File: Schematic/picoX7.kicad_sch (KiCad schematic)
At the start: 8 parts, among them J1 MIDI in, J2 Debug serial, SW1 RST, U1 H11L1, U2 Pico, U3 I2S DAC

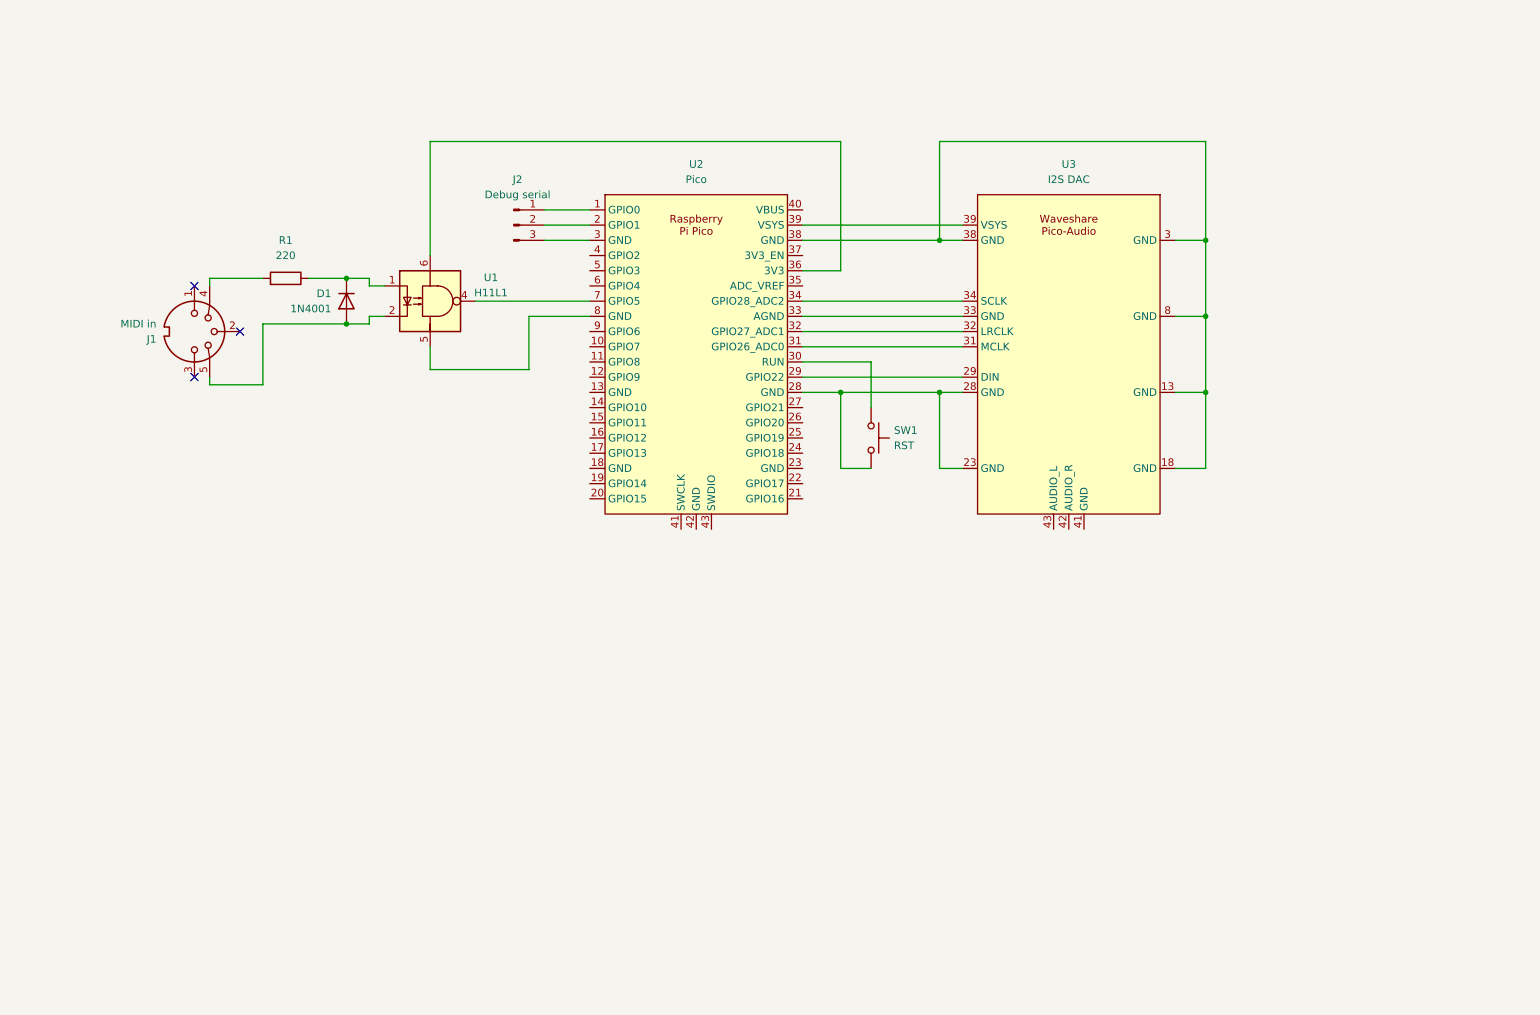
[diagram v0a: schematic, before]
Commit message: Update schematic with planned extensions
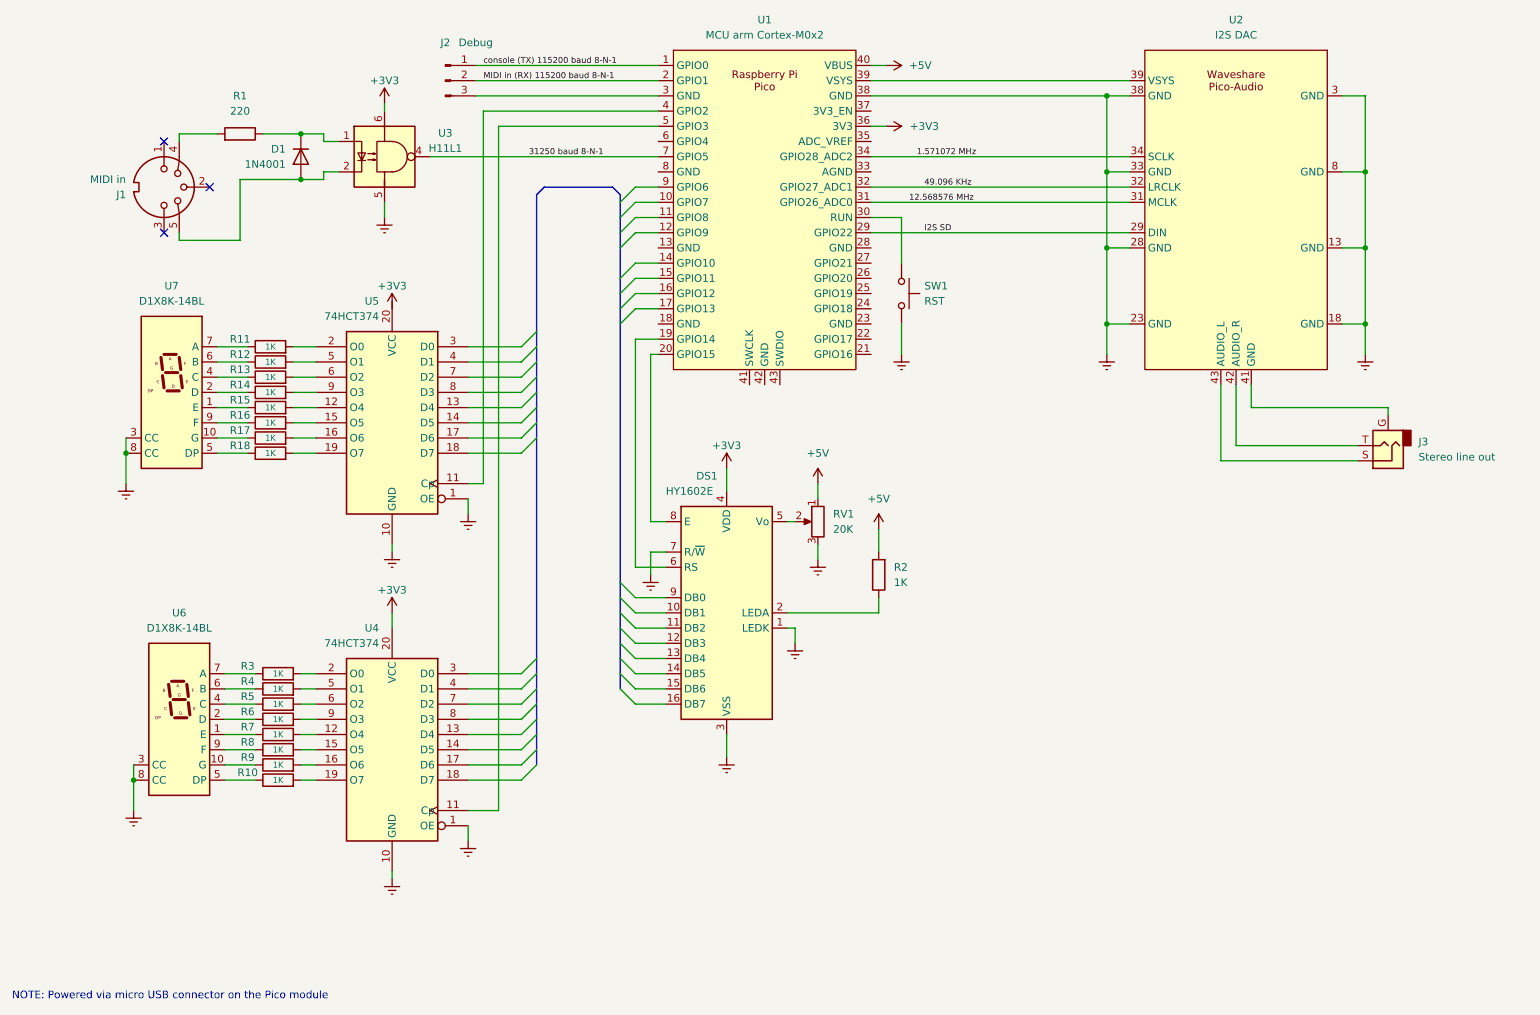
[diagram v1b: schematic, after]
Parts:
- added DS1: HY1602E, Display:HY1602E, symbol Display_Character:HY1602E
- added J3: Stereo line out, symbol Connector_Audio:AudioJack2_Ground
- added R10, R11, R12, R13, R14, R15, R16, R17, R18, R2, R3, R4, R5, R6, R7, R8, R9: 1K, Resistor_THT:R_Axial_DIN0204_L3.6mm_D1.6mm_P5.08mm_Horizontal, symbol Device:R
- added RV1: 20K, symbol Device:R_Potentiometer
- added U4, U5: 74HCT374, symbol 74xx:74HCT374
- added U6, U7: D1X8K-14BL, Display_7Segment:D1X8K, symbol Display_Character:D1X8K-14BL
- J2: value Debug serial -> Debug
- U1: renamed from U2; value Pico -> MCU arm Cortex-M0x2
- renumbered U3 to U2, U1 to U3
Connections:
- net console (TX) 115200 baud 8-N-1: now reaches J2.1 (Pin_1), U1.1 (GPIO0)
- net MIDI in (RX) 115200 baud 8-N-1: now reaches J2.2 (Pin_2), U1.2 (GPIO1)
- net 31250 baud 8-N-1: now reaches U1.7 (GPIO5), U3.4
- net at U1.8 (GND): no longer U3.5
- net +3V3: now reaches U1.36 (3V3), U3.6
- net +3V3: now also DS1.4 (VDD), U4.20 (VCC)
- net Earth: now reaches SW1.2, U2.23 (GND), U2.28 (GND)
- net Earth: now also U1.38 (GND), U2.13 (GND), U2.18 (GND), U2.3 (GND), U2.33 (GND), U2.38 (GND), U2.8 (GND), U3.5, DS1.1 (LEDK), DS1.3 (VSS), DS1.7 (R/~{W}), RV1.3, U4.1 (OE), U4.10 (GND), U5.1 (OE), U5.10 (GND), U6.3 (CC), U6.8 (CC), U7.3 (CC), U7.8 (CC); no longer U1.28 (GND)
- net I2S SD: now reaches U1.29 (GPIO22), U2.29 (DIN)
- net 12.568576 MHz: now reaches U1.31 (GPIO26_ADC0), U2.31 (MCLK)
- net 49.096 KHz: now reaches U1.32 (GPIO27_ADC1), U2.32 (LRCLK)
- net at U1.33 (AGND): no longer U2.33 (GND)
- net 1.571072 MHz: now reaches U1.34 (GPIO28_ADC2), U2.34 (SCLK)
- net at U2.41 (GND): now also J3.G
- net at U2.42 (AUDIO_R): now also J3.T
- net at U2.43 (AUDIO_L): now also J3.S
- net at U1.19 (GPIO14): now also DS1.6 (RS)
- net at U1.20 (GPIO15): now also DS1.8 (E)
- net at U1.4 (GPIO2): now also U5.11 (Cp)
- net +5V: now reaches U1.40 (VBUS)
- net +5V: now also R2.2, RV1.1
- net at U1.5 (GPIO3): now also U4.11 (Cp)
- new net: R9.1, U6.10 (G)
- new net: R9.2, U4.16 (O6)
- new net: R15.1, U7.1 (E)
- new net: R17.1, U7.10 (G)
- new net: R14.1, U7.2 (D)
- new net: R13.1, U7.4 (C)
- new net: R18.1, U7.5 (DP)
- new net: R12.1, U7.6 (B)
- new net: R11.1, U7.7 (A)
- new net: R16.1, U7.9 (F)
- new net: R7.2, U4.12 (O4)
- new net: R8.2, U4.15 (O5)
- new net: R10.2, U4.19 (O7)
- new net: R3.2, U4.2 (O0)
- new net: R4.2, U4.5 (O1)
- new net: R5.2, U4.6 (O2)
- new net: R6.2, U4.9 (O3)
- new net: R11.2, U5.2 (O0)
- new net: R13.2, U5.6 (O2)
- new net: R18.2, U5.19 (O7)
- new net: R8.1, U6.9 (F)
- new net: R10.1, U6.5 (DP)
- new net: R14.2, U5.9 (O3)
- new net: R4.1, U6.6 (B)
- new net: DS1.5 (Vo), RV1.2
- new net: R6.1, U6.2 (D)
- new net: DS1.2 (LEDA), R2.1
- new net: R5.1, U6.4 (C)
- new net: R12.2, U5.5 (O1)
- new net: R15.2, U5.12 (O4)
- new net: R16.2, U5.15 (O5)
- new net: R17.2, U5.16 (O6)
- new net: R3.1, U6.7 (A)
- new net: R7.1, U6.1 (E)
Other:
- note added: "NOTE: Powered via micro USB connector on the Pico module"
- company: John Haughton -> https://github.com/AnotherJohnH/picoX7
- moved on the sheet: D1, J1, J2, R1, SW1, U1, U2, U3

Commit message: Update schematic to reflect changes to LED display
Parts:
- removed R2: 1K, Resistor_THT:R_Axial_DIN0204_L3.6mm_D1.6mm_P5.08mm_Horizontal, symbol Device:R
- removed U4, U5: 74HCT374, symbol 74xx:74HCT374
- added J4: Debug, Connector:FanPinHeader_1x03_P2.54mm_Vertical, symbol Connector:Conn_01x03_Pin
- added U4, U8: 74HCT164, symbol 74xx:74HCT164
- J3: footprint (none) -> Connector_Audio:Jack_3.5mm_CUI_SJ1-3523N_Horizontal
- R10, R11, R12, R13, R14, R15, R16, R17, R18, R3, R4, R5, R6, R7, R8, R9: value 1K -> 330
- SW1: footprint (none) -> Button_Switch_THT:SW_PUSH_6mm_H5mm
- U1, U2: footprint RPi_Pico:RPi_Pico_SMD_TH -> Package_DIP:DIP-40_W25.4mm_Socket_LongPads
- U3: footprint Package_DIP:DIP-6_W7.62mm -> Package_DIP:DIP-6_W7.62mm_LongPads
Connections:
- net +3V3: now also U4.14 (VCC), U4.9 (~{MR}), U8.14 (VCC), U8.9 (~{MR}); no longer DS1.4 (VDD)
- net +5V: now also DS1.2 (LEDA), DS1.4 (VDD)
- net Earth: now also U4.7 (GND), U8.7 (GND)
- net at R9.2: now also U4.13 (Q7)
- net at U1.5 (GPIO3): now also U4.8 (CP), U8.8 (CP)
- net at R7.2: now also U4.3 (Q0)
- net at R8.2: now also U4.12 (Q6)
- net at R10.2: now also U4.6 (Q3)
- net at R3.2: now also U4.11 (Q5)
- net at R4.2: now also U4.10 (Q4)
- net at R5.2: now also U4.5 (Q2)
- net at R6.2: now also U4.4 (Q1)
- net at R11.2: now also U8.11 (Q5)
- net at R13.2: now also U8.5 (Q2)
- net at R18.2: now also U8.6 (Q3)
- net at R14.2: now also U8.4 (Q1)
- net at R12.2: now also U8.10 (Q4)
- net D1: now reaches DS1.10 (DB1)
- net D1: now also U1.10 (GPIO7)
- net D2: now reaches DS1.11 (DB2)
- net D2: now also U1.11 (GPIO8)
- net D3: now reaches DS1.12 (DB3)
- net D3: now also U1.12 (GPIO9)
- net D4: now reaches DS1.13 (DB4)
- net D4: now also U1.14 (GPIO10)
- net D5: now reaches DS1.14 (DB5)
- net D5: now also U1.15 (GPIO11)
- net D6: now reaches DS1.15 (DB6)
- net D6: now also U1.16 (GPIO12)
- net D7: now reaches DS1.16 (DB7)
- net D7: now also U1.17 (GPIO13)
- net D0: now reaches DS1.9 (DB0)
- net D0: now also U1.9 (GPIO6)
- net at U1.4 (GPIO2): now also U8.1 (DSA), U8.2 (DSB)
- net at R15.2: now also U8.3 (Q0)
- net at R16.2: now also U8.12 (Q6)
- net at R17.2: now also U4.1 (DSA), U4.2 (DSB), U8.13 (Q7)
- net at U1.41 (SWCLK): now also J4.1 (Pin_1)
- net at U1.42 (GND): now also J4.2 (Pin_2)
- net at U1.43 (SWDIO): now also J4.3 (Pin_3)
- no-connect marks 3 -> 5
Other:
- moved on the sheet: DS1, R10, R11, R12, R13, R14, R15, R16, R17, R18, R3, R4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

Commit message: Minor schematic update
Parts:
- added R2: 470, Resistor_THT:R_Axial_DIN0204_L3.6mm_D1.6mm_P5.08mm_Horizontal, symbol Device:R
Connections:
- net +5V: now also R2.1; no longer DS1.2 (LEDA)
- new net: DS1.2 (LEDA), R2.2
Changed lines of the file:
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@@
   (title_block
     (title "picoX7")
-    (date "2023-08-30")
+    (date "2023-09-05")
     (rev "0.03")
     (company "https://github.com/AnotherJohnH/picoX7")
@@
     (stroke (width 0) (type default))
   )
+  (wire (pts (xy 149.86 134.62) (xy 153.67 134.62))
+    (stroke (width 0) (type default))
+  )
+  (wire (pts (xy 161.29 134.62) (xy 165.1 134.62))
+    (stroke (width 0) (type default))
+  )
   (wire (pts (xy 36.83 95.25) (xy 36.83 71.12))
     (stroke (width 0) (type default))
@@
     (stroke (width 0) (type default))
   )
-  (wire (pts (xy 149.86 134.62) (xy 163.83 134.62))
-    (stroke (width 0) (type default))
-  )
   (wire (pts (xy 93.98 95.25) (xy 88.9 95.25))
     (stroke (width 0) (type default))
@@
     (stroke (width 0) (type default))
   )
-  (wire (pts (xy 163.83 132.08) (xy 163.83 134.62))
+  (wire (pts (xy 165.1 132.08) (xy 165.1 134.62))
     (stroke (width 0) (type default))
   )
@@
     )
   )
-  (symbol (lib_id "power:+5V") (at 163.83 132.08 0) (mirror y) (unit 1)
-    (in_bom yes) (on_board yes) (dnp no)
-    (property "Reference" "#PWR013" (at 163.83 135.89 0)
-      (effects (font (size 1.27 1.27)) hide)
-    )
-    (property "Value" "+5V" (at 163.83 127 0)
-      (effects (font (size 1.27 1.27)))
-    )
-    (property "Footprint" "" (at 163.83 132.08 0)
-      (effects (font (size 1.27 1.27)) hide)
-    )
-    (property "Datasheet" "" (at 163.83 132.08 0)
+  (symbol (lib_id "power:+5V") (at 165.1 132.08 0) (mirror y) (unit 1)
+    (in_bom yes) (on_board yes) (dnp no)
+    (property "Reference" "#PWR013" (at 165.1 135.89 0)
+      (effects (font (size 1.27 1.27)) hide)
+    )
+    (property "Value" "+5V" (at 165.1 127 0)
+      (effects (font (size 1.27 1.27)))
+    )
+    (property "Footprint" "" (at 165.1 132.08 0)
+      (effects (font (size 1.27 1.27)) hide)
+    )
+    (property "Datasheet" "" (at 165.1 132.08 0)
       (effects (font (size 1.27 1.27)) hide)
     )
@@
         )
       )
+    )
+  )
+  (symbol (lib_id "Device:R") (at 157.48 134.62 270) (mirror x) (unit 1)
+    (in_bom yes) (on_board yes) (dnp no)
+    (property "Reference" "R2" (at 162.56 133.35 90)
+      (effects (font (size 1.27 1.27)))
+    )
+    (property "Value" "470" (at 157.48 134.62 90)
+      (effects (font (size 1 1)))
+    )
+    (property "Footprint" "Resistor_THT:R_Axial_DIN0204_L3.6mm_D1.6mm_P5.08mm_Horizontal" (at 157.48 136.398 90)
+      (effects (font (size 1.27 1.27)) hide)
+    )
+    (property "Datasheet" "~" (at 157.48 134.62 0)
+      (effects (font (size 1.27 1.27)) hide)
+    )
+    (pin "1")
+    (pin "2")
+    (instances
+      (project "picoX7"
+        (path "/8dd66cb3-bd85-43a0-9ef0-1bd8a27e677c"
+          (reference "R2") (unit 1)
+        )
+      )
